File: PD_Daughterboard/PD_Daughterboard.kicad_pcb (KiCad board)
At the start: 2 copper layers, 6.5 x 6 mm, 5 parts, among them J1 Conn_01x01_Pin, J2 Conn_01x01_Pin, J3 Conn_01x01_Pin, J4 Conn_01x01_Pin

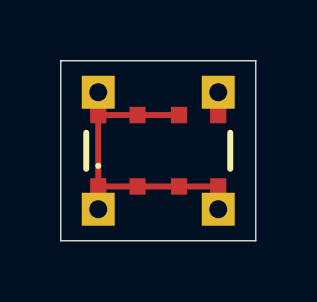
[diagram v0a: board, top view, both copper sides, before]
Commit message: add tmp daughter board
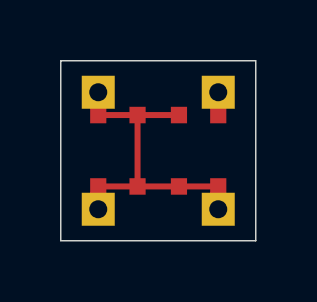
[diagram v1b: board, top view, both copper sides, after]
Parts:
- D1: footprint PD_Daughterboard:VEMD8082 -> PD_Daughterboard:VEMD8082C
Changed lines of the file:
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@@
 		(embedded_fonts no)
 	)
-	(footprint "PD_Daughterboard:VEMD8082"
+	(footprint "PD_Daughterboard:VEMD8082C"
 		(layer "F.Cu")
 		(at 150 100)
@@
 			)
 		)
-		(property "Datasheet" "https://www.vishay.com/docs/80381/vemd8082.pdf"
-			(at 0 0 0)
-			(layer "F.Fab")
-			(hide yes)
-			(effects
-				(font
-					(size 1.27 1.27)
-				)
-			)
-		)
-		(property "Description" "Photodiode 130 8-SMD, No Lead 350nm ~ 1100nm 20 V"
+		(property "Datasheet" ""
+			(at 0 0 0)
+			(layer "F.Fab")
+			(hide yes)
+			(effects
+				(font
+					(size 1.27 1.27)
+				)
+			)
+		)
+		(property "Description" ""
 			(at 0 0 0)
 			(layer "F.Fab")
@@
 		(sheetname "/")
 		(sheetfile "PD_Daughterboard.kicad_sch")
-		(units
-			(unit
-				(name "A")
-				(pins "1" "2" "3" "4" "8" "7" "6" "5")
-			)
-		)
 		(attr smd)
 		(duplicate_pad_numbers_are_jumpers no)
-		(fp_line
-			(start -2.4 -0.6)
-			(end -2.4 0.6)
-			(stroke
-				(width 0.2)
-				(type solid)
-			)
-			(layer "F.SilkS")
-		)
-		(fp_line
-			(start -2 0.45)
-			(end -2 0.45)
-			(stroke
-				(width 0.1)
-				(type solid)
-			)
-			(layer "F.SilkS")
-		)
-		(fp_line
-			(start -2 0.55)
-			(end -2 0.55)
-			(stroke
-				(width 0.1)
-				(type solid)
-			)
-			(layer "F.SilkS")
-		)
-		(fp_line
-			(start 2.4 -0.6)
-			(end 2.4 0.6)
-			(stroke
-				(width 0.2)
-				(type solid)
-			)
-			(layer "F.SilkS")
-		)
-		(fp_arc
-			(start -2 0.45)
-			(mid -1.95 0.5)
-			(end -2 0.55)
-			(stroke
-				(width 0.1)
-				(type solid)
-			)
-			(layer "F.SilkS")
-		)
-		(fp_arc
-			(start -2 0.55)
-			(mid -2.05 0.5)
-			(end -2 0.45)
-			(stroke
-				(width 0.1)
-				(type solid)
-			)
-			(layer "F.SilkS")
-		)
-		(fp_line
-			(start -2.4 -1.25)
-			(end 2.4 -1.25)
-			(stroke
-				(width 0.1)
-				(type solid)
-			)
-			(layer "F.Fab")
-		)
-		(fp_line
-			(start -2.4 1.25)
-			(end -2.4 -1.25)
-			(stroke
-				(width 0.1)
-				(type solid)
-			)
-			(layer "F.Fab")
-		)
-		(fp_line
-			(start 2.4 -1.25)
-			(end 2.4 1.25)
-			(stroke
-				(width 0.1)
-				(type solid)
-			)
-			(layer "F.Fab")
-		)
-		(fp_line
-			(start 2.4 1.25)
-			(end -2.4 1.25)
-			(stroke
-				(width 0.1)
-				(type solid)
-			)
-			(layer "F.Fab")
-		)
 		(pad "1" smd rect
 			(at -2 1.19)
@@
 	)
 	(segment
-		(start 148 98.81)
-		(end 148 101.19)
+		(start 149.31 98.81)
+		(end 149.31 101.19)
 		(width 0.2)
 		(layer "F.Cu")

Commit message: PD board space between leads synced with the one in main PCB
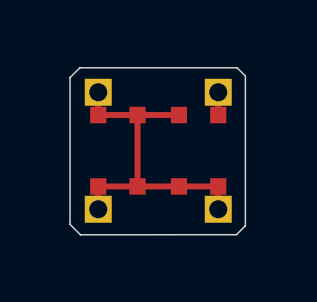
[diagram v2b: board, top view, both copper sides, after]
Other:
- board size 6.5 x 6 mm -> 5.8 x 5.6 mm
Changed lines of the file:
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@@
 		(pad "1" thru_hole rect
 			(at 0 0)
-			(size 1.1 1.1)
+			(size 0.9 0.9)
 			(drill 0.6)
 			(layers "*.Cu" "*.Mask")
@@
 		(pad "1" thru_hole rect
 			(at 0 0)
-			(size 1.1 1.1)
+			(size 0.9 0.9)
 			(drill 0.6)
 			(layers "*.Cu" "*.Mask")
@@
 		(pad "1" thru_hole rect
 			(at 0 0)
-			(size 1.1 1.1)
+			(size 0.9 0.9)
 			(drill 0.6)
 			(layers "*.Cu" "*.Mask")
@@
 		(pad "1" thru_hole rect
 			(at 0 0)
-			(size 1.1 1.1)
+			(size 0.9 0.9)
 			(drill 0.6)
 			(layers "*.Cu" "*.Mask")
@@
 		(embedded_fonts no)
 	)
-	(gr_rect
-		(start 146.75 97)
-		(end 153.25 103)
+	(gr_poly
+		(pts
+			(xy 152.905 102.5) (xy 152.606716 102.798284) (xy 147.406949 102.801725) (xy 147.059949 102.455177)
+			(xy 147.060051 97.559941) (xy 147.38521 97.234792) (xy 152.630203 97.235203) (xy 152.905 97.51)
+		)
 		(stroke
 			(width 0.05)
-			(type default)
+			(type solid)
 		)
 		(fill no)
